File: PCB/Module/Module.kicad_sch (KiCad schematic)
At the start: 24 parts, among them J1 SWD_Programmer, J2 Shield_Connector_Top_Right, J3 Shield_Connector_Bottom_Right, J4 Shield_Connector_Top_Left, J5 Shield_Connector_Bottom_Left, U1 PY32F002BF15P6TU, U2 PinHeaderTop, U3 PinHeaderRight, U4 PinHeaderBottom, U5 PinHeaderLeft

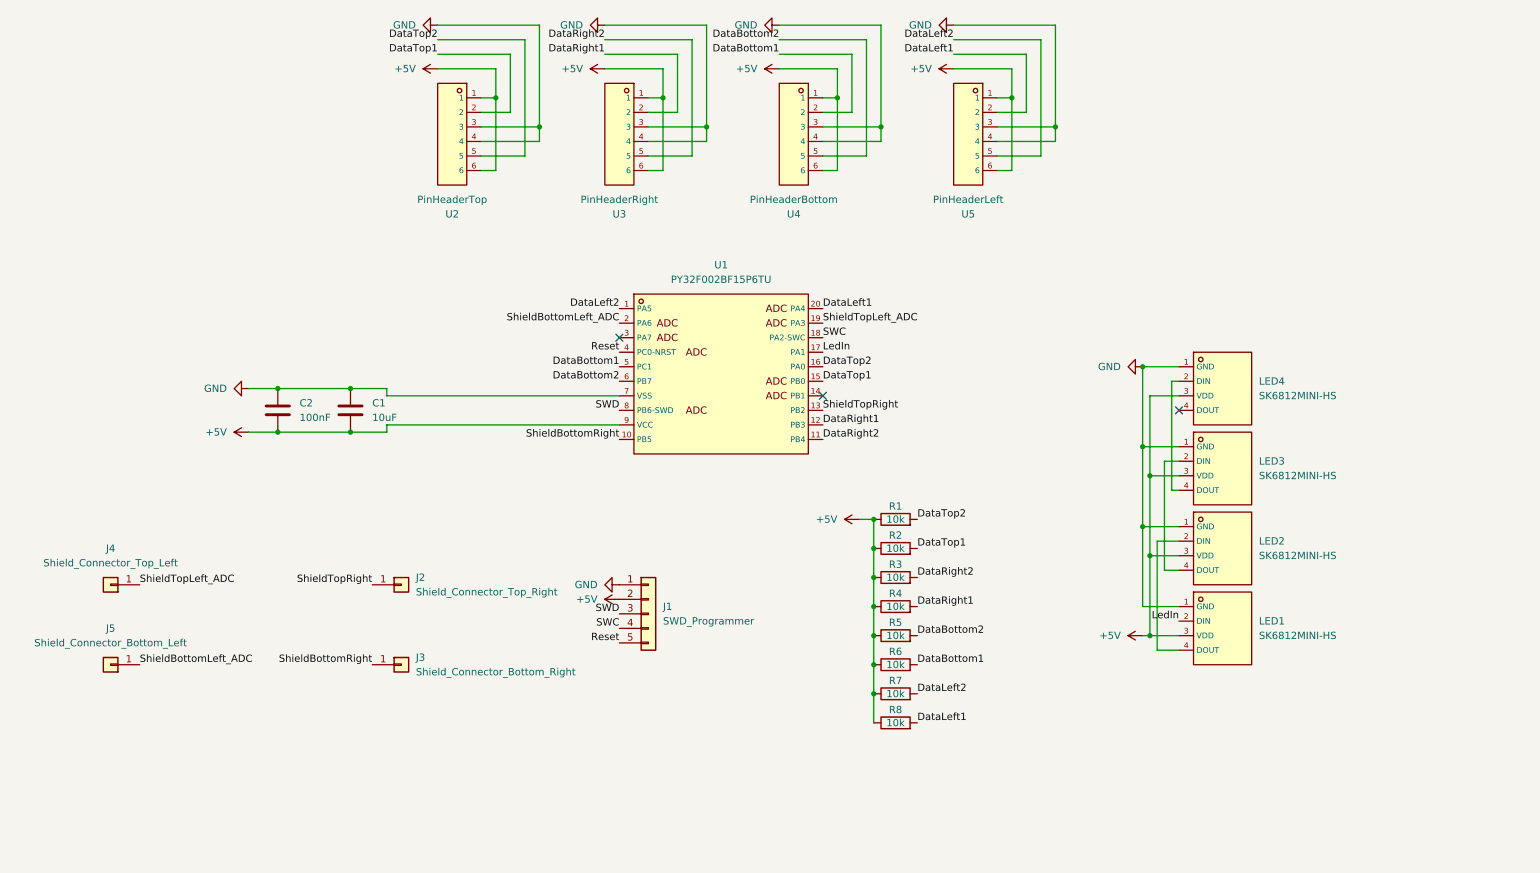
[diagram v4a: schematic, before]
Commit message: Finish module, power supply and connector design, panel is wip
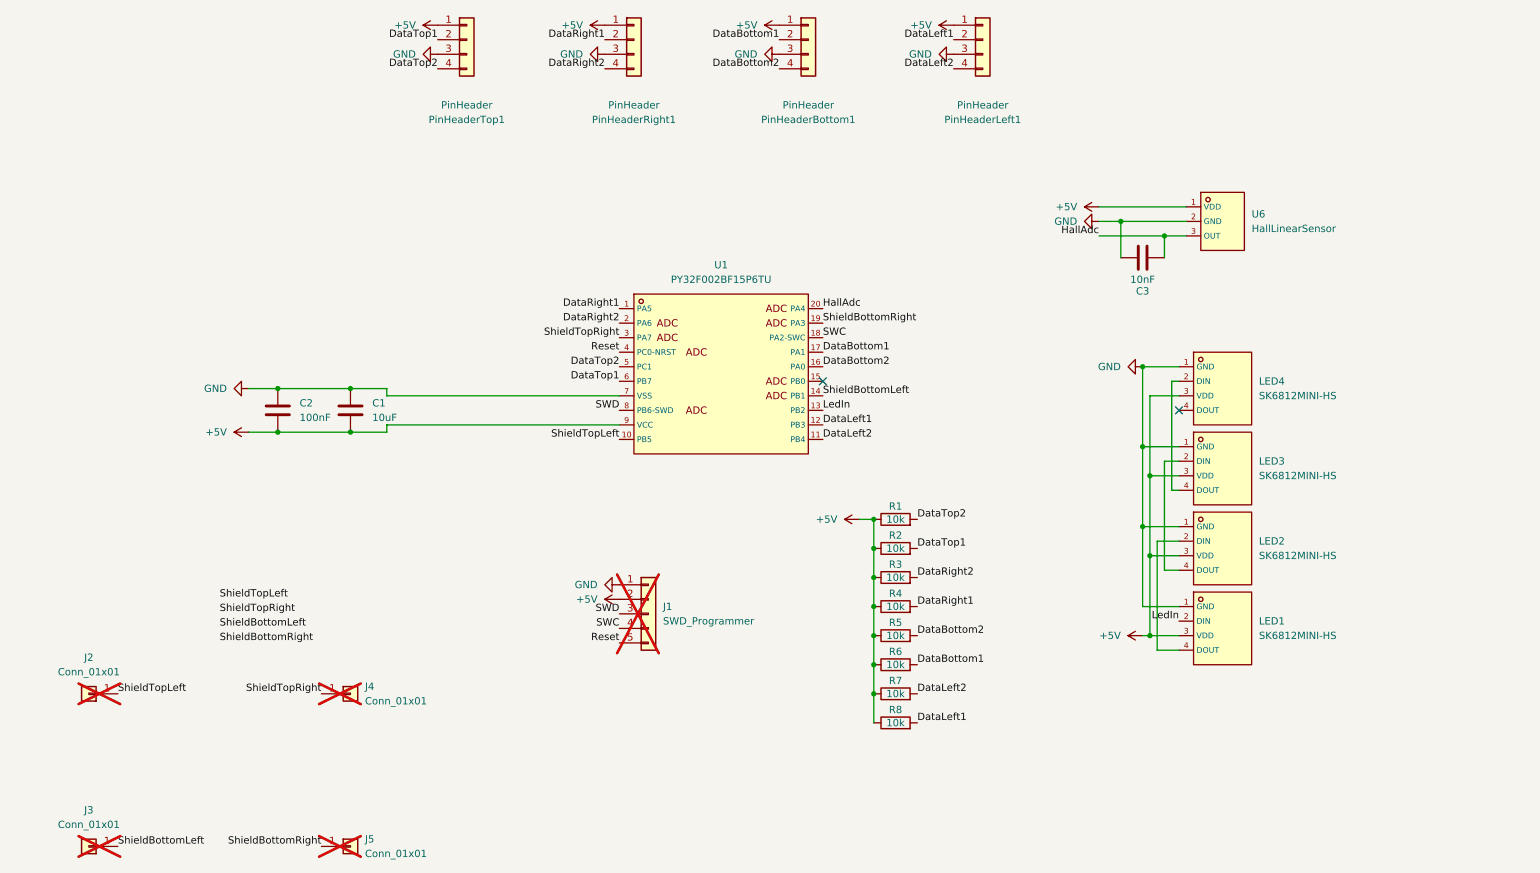
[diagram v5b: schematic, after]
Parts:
- added C3: 10nF, Capacitor_SMD:C_0402_1005Metric, symbol Device:C
- added U6: HallLinearSensor, CustomFootprints:HallLinearSensor, symbol Custom_Parts:HallLinearSensor
- C1: LCSC (none) -> C19702
- C2: LCSC (none) -> C1525
- J1: now not fitted
- J2: value Shield_Connector_Top_Right -> Conn_01x01; footprint CustomFootprints:HDR-TH_1P-V-F-1 -> CustomFootprints:ShieldConnector; LCSC C2883469 -> (none); now not fitted; now left out of the parts list
- J3: value Shield_Connector_Bottom_Right -> Conn_01x01; footprint CustomFootprints:HDR-TH_1P-V-F-1 -> CustomFootprints:ShieldConnector; LCSC C2883469 -> (none); now not fitted; now left out of the parts list
- J4: value Shield_Connector_Top_Left -> Conn_01x01; footprint CustomFootprints:HDR-TH_1P-V-F-1 -> CustomFootprints:ShieldConnector; LCSC C2883469 -> (none); now not fitted; now left out of the parts list
- J5: value Shield_Connector_Bottom_Left -> Conn_01x01; footprint CustomFootprints:HDR-TH_1P-V-F-1 -> CustomFootprints:ShieldConnector; LCSC C2883469 -> (none); now not fitted; now left out of the parts list
- PinHeaderBottom1: renamed from U4; value PinHeaderBottom -> PinHeader; footprint CustomFootprints:01x06_PinHeader_Angled -> CustomFootprints:01x04_PinPads; symbol Custom_Parts:01x06_PinHeader_Angled -> Connector_Generic:Conn_01x04; now left out of the parts list
- PinHeaderLeft1: renamed from U5; value PinHeaderLeft -> PinHeader; footprint CustomFootprints:01x06_PinHeader_Angled -> CustomFootprints:01x04_PinPads; symbol Custom_Parts:01x06_PinHeader_Angled -> Connector_Generic:Conn_01x04; now left out of the parts list
- PinHeaderRight1: renamed from U3; value PinHeaderRight -> PinHeader; footprint CustomFootprints:01x06_PinHeader_Angled -> CustomFootprints:01x04_PinPads; symbol Custom_Parts:01x06_PinHeader_Angled -> Connector_Generic:Conn_01x04; now left out of the parts list
- PinHeaderTop1: renamed from U2; value PinHeaderTop -> PinHeader; footprint CustomFootprints:01x06_PinHeader_Angled -> CustomFootprints:01x04_PinPads; symbol Custom_Parts:01x06_PinHeader_Angled -> Connector_Generic:Conn_01x04; now left out of the parts list
- R1, R2, R3, R4, R5, R6, R7, R8: LCSC (none) -> C25744
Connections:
- net +5V: now also U6.1 (VDD); no longer PinHeaderBottom1.6, PinHeaderLeft1.6, PinHeaderRight1.6, PinHeaderTop1.6
- net DataBottom1: now also U1.17 (PA1); no longer U1.5 (PC1)
- net DataBottom2: now also PinHeaderBottom1.4 (Pin_4), U1.16 (PA0); no longer PinHeaderBottom1.5, U1.6 (PB7)
- net DataLeft1: now also U1.12 (PB3); no longer U1.20 (PA4)
- net DataLeft2: now also PinHeaderLeft1.4 (Pin_4), U1.11 (PB4); no longer PinHeaderLeft1.5, U1.1 (PA5)
- net DataRight1: now also U1.1 (PA5); no longer U1.12 (PB3)
- net DataRight2: now also PinHeaderRight1.4 (Pin_4), U1.2 (PA6); no longer PinHeaderRight1.5, U1.11 (PB4)
- net DataTop1: now also U1.6 (PB7); no longer U1.15 (PB0)
- net DataTop2: now also PinHeaderTop1.4 (Pin_4), U1.5 (PC1); no longer PinHeaderTop1.5, U1.16 (PA0)
- net GND: now also C3.1, U6.2 (GND); no longer PinHeaderBottom1.4, PinHeaderLeft1.4, PinHeaderRight1.4, PinHeaderTop1.4
- net LedIn: now also U1.13 (PB2); no longer U1.17 (PA1)
- net ShieldBottomRight: now also J5.1 (Pin_1), U1.19 (PA3); no longer J3.1 (Pin_1), U1.10 (PB5)
- net ShieldTopRight: now also J4.1 (Pin_1), U1.3 (PA7); no longer J2.1 (Pin_1), U1.13 (PB2)
- net ShieldBottomLeft: now reaches U1.14 (PB1)
- net ShieldBottomLeft: now also J3.1 (Pin_1)
- removed net ShieldBottomLeft_ADC: J5.1 (Pin_1), U1.2 (PA6)
- removed net ShieldTopLeft_ADC: J4.1 (Pin_1), U1.19 (PA3)
- new net HallAdc: C3.2, U1.20 (PA4), U6.3 (OUT)
- new net ShieldTopLeft: J2.1 (Pin_1), U1.10 (PB5)
- no-connect marks 3 -> 2

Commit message: Finish panel script
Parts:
- PinHeaderBottom1, PinHeaderLeft1, PinHeaderRight1, PinHeaderTop1: now not fitted
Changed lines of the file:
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@@
 		(in_bom no)
 		(on_board yes)
-		(dnp no)
+		(dnp yes)
 		(property "Reference" "PinHeaderBottom1"
 			(at 160.02 39.37 0)
@@
 		(in_bom no)
 		(on_board yes)
-		(dnp no)
+		(dnp yes)
 		(property "Reference" "PinHeaderRight1"
 			(at 129.54 39.37 0)
@@
 		(in_bom no)
 		(on_board yes)
-		(dnp no)
+		(dnp yes)
 		(property "Reference" "PinHeaderTop1"
 			(at 100.33 39.37 0)
@@
 		(in_bom no)
 		(on_board yes)
-		(dnp no)
+		(dnp yes)
 		(property "Reference" "PinHeaderLeft1"
 			(at 190.5 39.37 0)

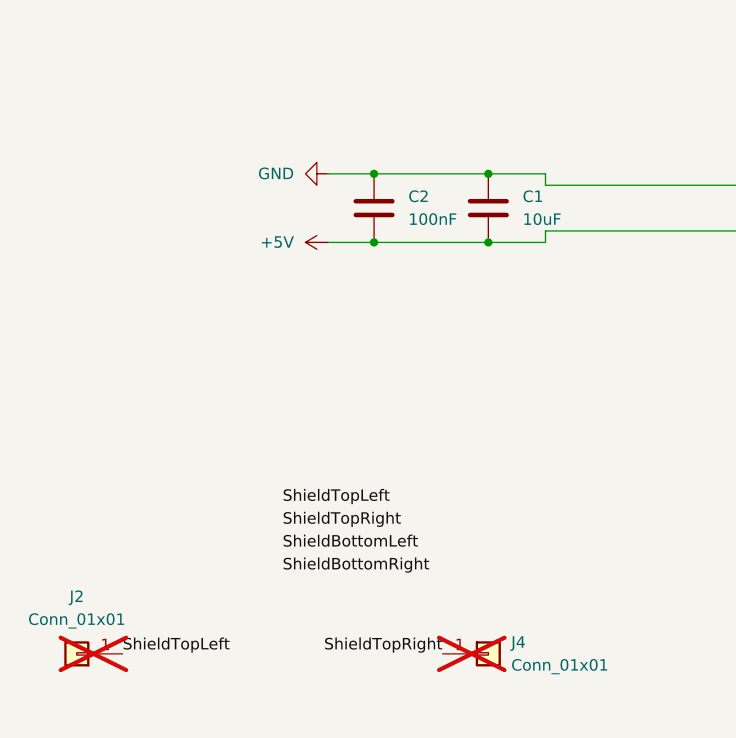
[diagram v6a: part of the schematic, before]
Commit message: Add electrolytic bulk capacitors to modules and power supply
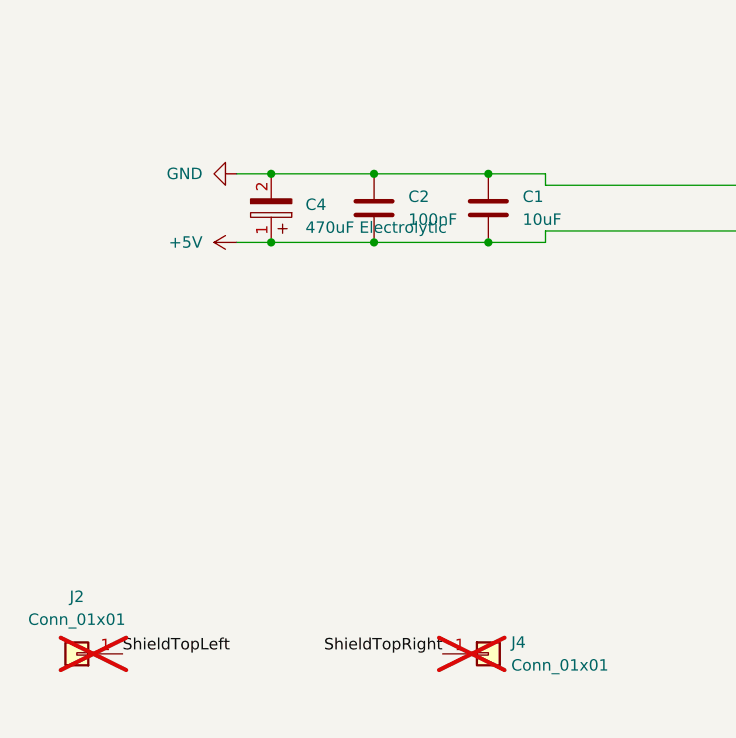
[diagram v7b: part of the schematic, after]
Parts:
- added C4: 470uF Electrolytic, CustomFootprints:CAP-SMD_BD6.3-L6.6-W6.6-FD, symbol Custom_Parts:ElectrolyticCapacitorSMD
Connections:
- net +5V: now also C4.1
- net GND: now also C4.2
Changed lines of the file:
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@@
 	)
 	(junction
+		(at 55.88 93.98)
+		(diameter 0)
+		(color 0 0 0 0)
+	)
+	(junction
 		(at 219.71 115.57)
 		(diameter 0)
@@
 	)
 	(junction
+		(at 55.88 86.36)
+		(diameter 0)
+		(color 0 0 0 0)
+	)
+	(junction
 		(at 171.45 134.62)
 		(diameter 0)
@@
 	(wire
 		(pts
+			(xy 55.88 86.36) (xy 67.31 86.36)
+		)
+		(stroke
+			(width 0)
+			(type default)
+		)
+	)
+	(wire
+		(pts
 			(xy 222.25 59.69) (xy 226.06 59.69)
 		)
@@
 	(wire
 		(pts
+			(xy 55.88 93.98) (xy 67.31 93.98)
+		)
+		(stroke
+			(width 0)
+			(type default)
+		)
+	)
+	(wire
+		(pts
 			(xy 171.45 109.22) (xy 171.45 114.3)
 		)
@@
 	(wire
 		(pts
-			(xy 62.23 93.98) (xy 67.31 93.98)
-		)
-		(stroke
-			(width 0)
-			(type default)
-		)
-	)
-	(wire
-		(pts
 			(xy 224.79 132.08) (xy 220.98 132.08)
 		)
@@
 	(wire
 		(pts
-			(xy 62.23 86.36) (xy 67.31 86.36)
-		)
-		(stroke
-			(width 0)
-			(type default)
-		)
-	)
-	(wire
-		(pts
 			(xy 171.45 129.54) (xy 171.45 134.62)
 		)
@@
 	(wire
 		(pts
+			(xy 52.07 86.36) (xy 55.88 86.36)
+		)
+		(stroke
+			(width 0)
+			(type default)
+		)
+	)
+	(wire
+		(pts
 			(xy 171.45 134.62) (xy 171.45 139.7)
 		)
@@
 	(wire
 		(pts
+			(xy 52.07 93.98) (xy 55.88 93.98)
+		)
+		(stroke
+			(width 0)
+			(type default)
+		)
+	)
+	(wire
+		(pts
 			(xy 171.45 124.46) (xy 171.45 129.54)
 		)
@@
 		)
 	)
-	(label "ShieldBottomRight"
-		(at 57.15 130.81 0)
-		(effects
-			(font
-				(size 1.27 1.27)
-			)
-			(justify left bottom)
-		)
-	)
-	(label "ShieldTopRight"
-		(at 57.15 125.73 0)
-		(effects
-			(font
-				(size 1.27 1.27)
-			)
-			(justify left bottom)
-		)
-	)
 	(label "DataTop1"
 		(at 179.07 114.3 0)
@@
 		)
 	)
-	(label "ShieldBottomLeft"
-		(at 57.15 128.27 0)
-		(effects
-			(font
-				(size 1.27 1.27)
-			)
-			(justify left bottom)
-		)
-	)
 	(label "DataBottom1"
 		(at 162.56 80.01 0)
@@
 		)
 	)
-	(label "ShieldTopLeft"
-		(at 57.15 123.19 0)
-		(effects
-			(font
-				(size 1.27 1.27)
-			)
-			(justify left bottom)
-		)
-	)
 	(label "DataLeft2"
 		(at 179.07 139.7 0)
@@
 	)
 	(symbol
+		(lib_id "Custom_Parts:ElectrolyticCapacitorSMD")
+		(at 55.88 90.17 180)
+		(unit 1)
+		(exclude_from_sim no)
+		(in_bom yes)
+		(on_board yes)
+		(dnp no)
+		(fields_autoplaced yes)
+		(property "Reference" "C4"
+			(at 59.69 89.7889 0)
+			(effects
+				(font
+					(size 1.27 1.27)
+				)
+				(justify right)
+			)
+		)
+		(property "Value" "470uF Electrolytic"
+			(at 59.69 92.3289 0)
+			(effects
+				(font
+					(size 1.27 1.27)
+				)
+				(justify right)
+			)
+		)
+		(property "Footprint" "CustomFootprints:CAP-SMD_BD6.3-L6.6-W6.6-FD"
+			(at 55.88 80.01 0)
+			(effects
+				(font
+					(size 1.27 1.27)
+					(italic yes)
+				)
+				(hide yes)
+			)
+		)
+		(property "Datasheet" "https://item.szlcsc.com/265679.html"
+			(at 58.166 90.297 0)
+			(effects
+				(font
+					(size 1.27 1.27)
+				)
+				(justify left)
+				(hide yes)
+			)
+		)
+		(property "Description" ""
+			(at 55.88 90.17 0)
+			(effects
+				(font
+					(size 1.27 1.27)
+				)
+				(hide yes)
+			)
+		)
+		(property "LCSC" "C335982"
+			(at 55.88 90.17 0)
+			(effects
+				(font
+					(size 1.27 1.27)
+				)
+				(hide yes)
+			)
+		)
+		(pin "1"
+		)
+		(pin "2"
+		)
+		(instances
+			(project ""
+				(path "/2afdbff6-2171-4e7e-8bad-f5e58bc69363"
+					(reference "C4")
+					(unit 1)
+				)
+			)
+		)
+	)
+	(symbol
 		(lib_id "Connector_Generic:Conn_01x01")
 		(at 80.01 139.7 0)
@@
 	(symbol
 		(lib_id "power:GND")
-		(at 62.23 86.36 270)
+		(at 52.07 86.36 270)
 		(unit 1)
 		(exclude_from_sim no)
@@
 		(fields_autoplaced yes)
 		(property "Reference" "#PWR1"
-			(at 55.88 86.36 0)
+			(at 45.72 86.36 0)
 			(effects
 				(font
@@
 		)
 		(property "Value" "GND"
-			(at 58.42 86.3599 90)
+			(at 48.26 86.3599 90)
 			(effects
 				(font
@@
 		)
 		(property "Footprint" ""
-			(at 62.23 86.36 0)
+			(at 52.07 86.36 0)
 			(effects
 				(font
@@
 		)
 		(property "Datasheet" ""
-			(at 62.23 86.36 0)
+			(at 52.07 86.36 0)
 			(effects
 				(font
@@
 		)
 		(property "Description" "Power symbol creates a global label with name \"GND\" , ground"
-			(at 62.23 86.36 0)
+			(at 52.07 86.36 0)
 			(effects
 				(font
@@
 	(symbol
 		(lib_id "power:+5V")
-		(at 62.23 93.98 90)
+		(at 52.07 93.98 90)
 		(unit 1)
 		(exclude_from_sim no)
@@
 		(fields_autoplaced yes)
 		(property "Reference" "#PWR2"
-			(at 66.04 93.98 0)
+			(at 55.88 93.98 0)
 			(effects
 				(font
@@
 		)
 		(property "Value" "+5V"
-			(at 58.42 93.9799 90)
+			(at 48.26 93.9799 90)
 			(effects
 				(font
@@
 		)
 		(property "Footprint" ""
-			(at 62.23 93.98 0)
+			(at 52.07 93.98 0)
 			(effects
 				(font
@@
 		)
 		(property "Datasheet" ""
-			(at 62.23 93.98 0)
+			(at 52.07 93.98 0)
 			(effects
 				(font
@@
 		)
 		(property "Description" "Power symbol creates a global label with name \"+5V\""
-			(at 62.23 93.98 0)
+			(at 52.07 93.98 0)
 			(effects
 				(font
